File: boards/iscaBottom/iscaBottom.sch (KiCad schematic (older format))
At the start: 30 parts, among them J1 CONN_01X36, J2 CONN_01X36, J3 CONN_01X36

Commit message: iscaBottom: v2 electricly complete
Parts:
- RTD15: footprint footprints:4wire_SMDsolder -> footprints:4wire_SMDsolder_reverse
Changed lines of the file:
@@
 LIBS:valves
 LIBS:lib_iscaBottom
+LIBS:iscaBottom-cache
 EELAYER 25 0
 EELAYER END
@@
 F 0 "RTD15" V 1350 6650 50  0000 C CNN
 F 1 "RTD_4WIRE" V 1450 6650 50  0000 C CNN
-F 2 "footprints:4wire_SMDsolder" H 1550 6650 50  0001 C CNN
+F 2 "footprints:4wire_SMDsolder_reverse" H 1550 6650 50  0001 C CNN
 F 3 "" H 1550 6650 50  0001 C CNN
 	1    1550 6650

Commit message: iscaBottom: board_completed
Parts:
- added R1: 0, Resistors_SMD:R_0603_HandSoldering, symbol R
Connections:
- new net shield: R1.1, R1.2
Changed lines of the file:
@@
 Wire Wire Line
 	1850 8000 2100 8000
+Wire Wire Line
+	3200 800  3750 800
+Text Label 3450 800  0    60   ~ 0
+shield
+$Comp
+L R R1
+U 1 1 59ED224A
+P 3450 900
+F 0 "R1" V 3530 900 50  0000 C CNN
+F 1 "0" V 3450 900 50  0000 C CNN
+F 2 "Resistors_SMD:R_0603_HandSoldering" V 3380 900 50  0001 C CNN
+F 3 "" H 3450 900 50  0001 C CNN
+	1    3450 900
+	0    1    1    0
+$EndComp
+Wire Wire Line
+	3750 800  3750 900
+Wire Wire Line
+	3750 900  3600 900
+Wire Wire Line
+	3200 800  3200 900
+Wire Wire Line
+	3200 900  3300 900
 $EndSCHEMATC

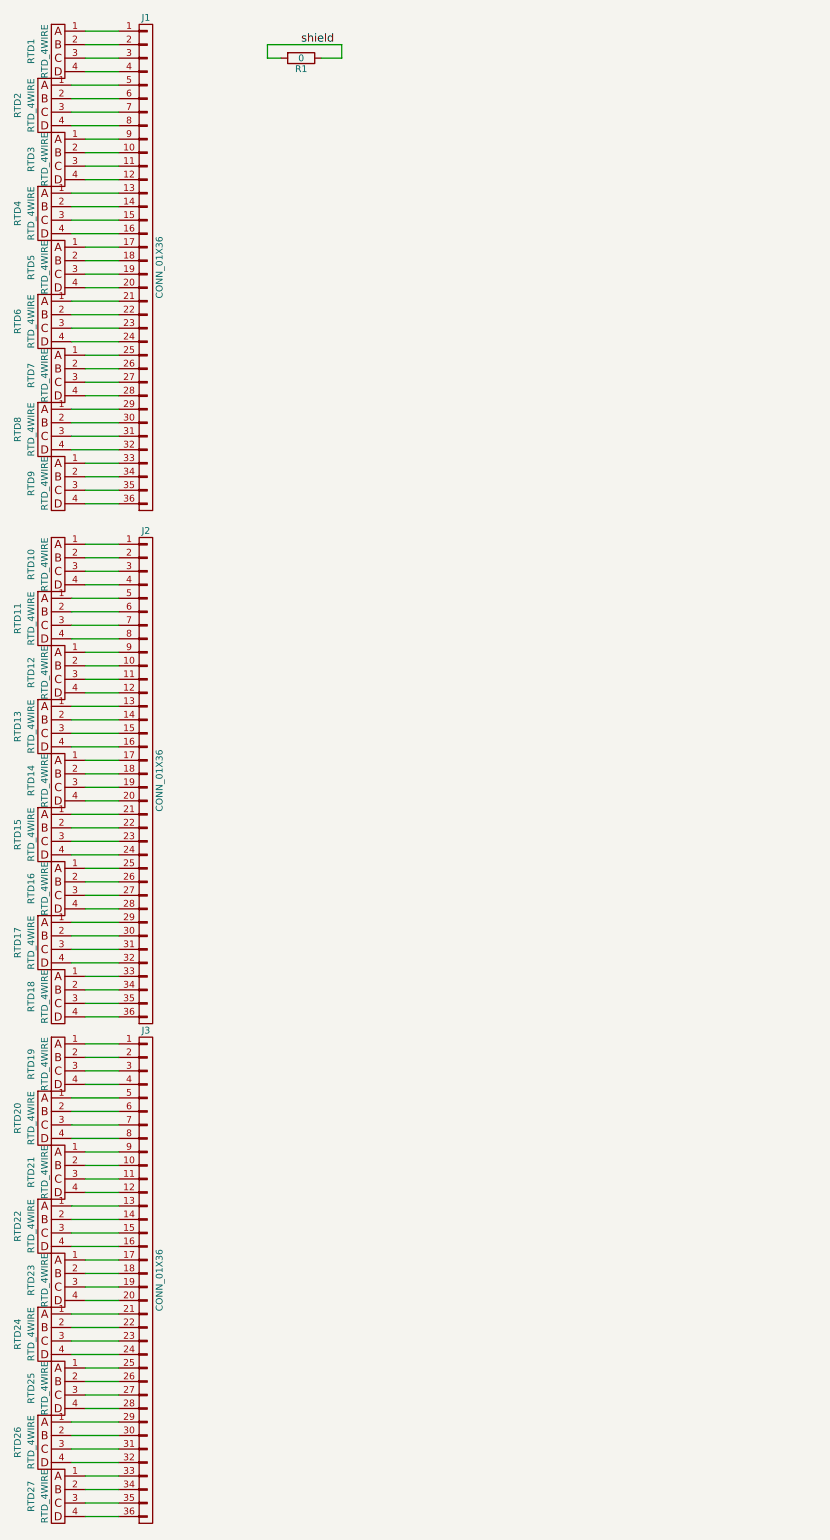
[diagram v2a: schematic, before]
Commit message: addressed all the errors
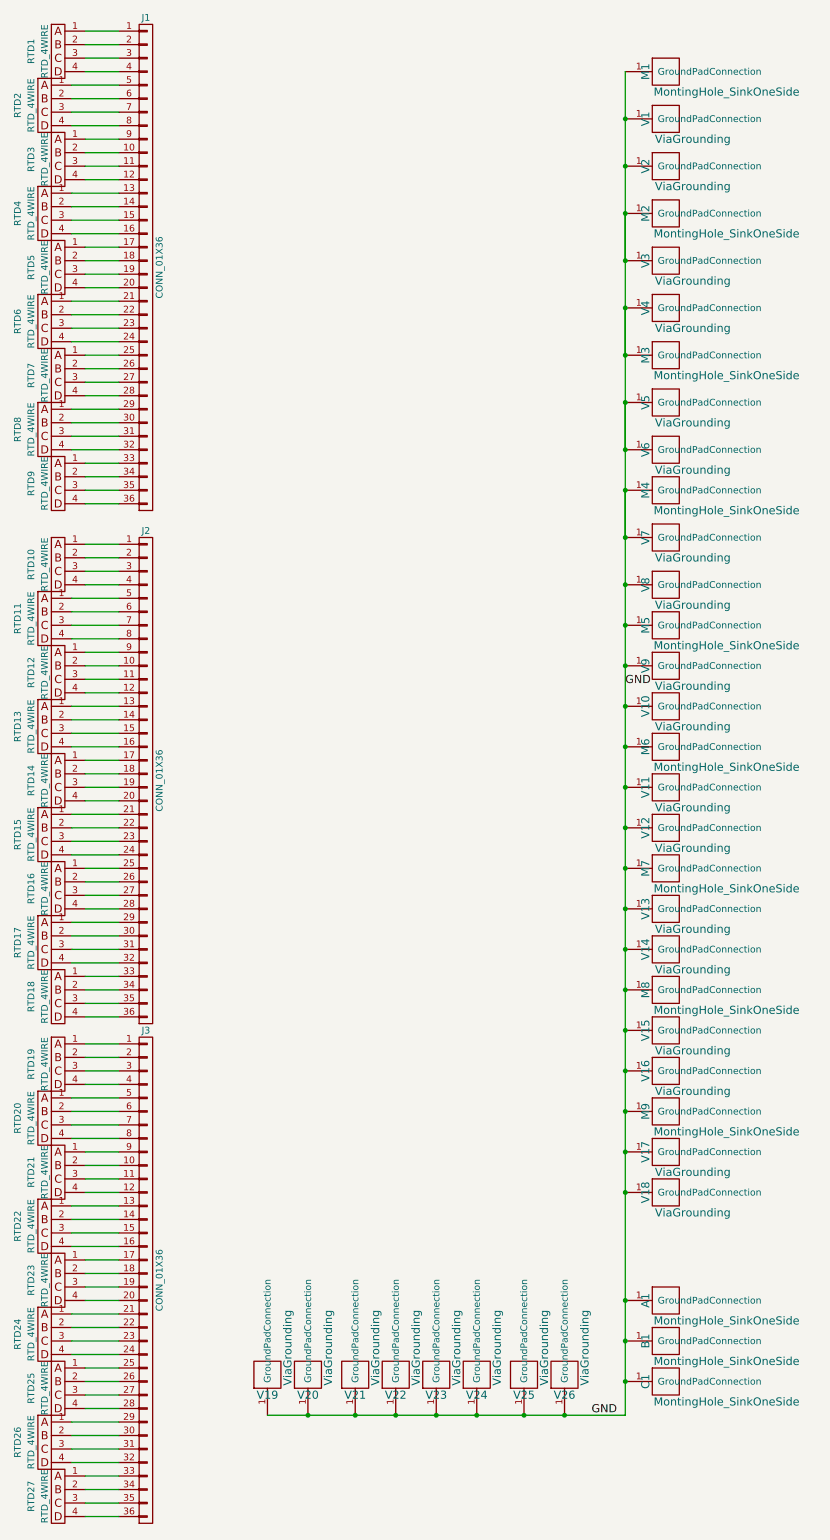
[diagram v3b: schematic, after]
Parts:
- removed R1: 0, Resistors_SMD:R_0603_HandSoldering, symbol R
- added A1, B1, C1, M1, M2, M3, M4, M5, M6, M7, M8, M9: MontingHole_SinkOneSide, footprints:MountingHoleM2_2.2mm_oneSided, symbol MontingHole_SinkOneSide
- added V1, V10, V11, V12, V13, V14, V15, V16, V17, V18, V19, V2, V20, V21, V22, V23, V24, V25, V26, V3, V4, V5, V6, V7, V8, V9: ViaGrounding, footprints:GroundingVia, symbol ViaGrounding
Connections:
- new net GND: A1.1 (GroundPadConnection), B1.1 (GroundPadConnection), C1.1 (GroundPadConnection), M1.1 (GroundPadConnection), M2.1 (GroundPadConnection), M3.1 (GroundPadConnection), M4.1 (GroundPadConnection), M5.1 (GroundPadConnection), M6.1 (GroundPadConnection), M7.1 (GroundPadConnection), M8.1 (GroundPadConnection), M9.1 (GroundPadConnection), V1.1 (GroundPadConnection), V10.1 (GroundPadConnection), V11.1 (GroundPadConnection), V12.1 (GroundPadConnection), V13.1 (GroundPadConnection), V14.1 (GroundPadConnection), V15.1 (GroundPadConnection), V16.1 (GroundPadConnection), V17.1 (GroundPadConnection), V18.1 (GroundPadConnection), V19.1 (GroundPadConnection), V2.1 (GroundPadConnection), V20.1 (GroundPadConnection), V21.1 (GroundPadConnection), V22.1 (GroundPadConnection), V23.1 (GroundPadConnection), V24.1 (GroundPadConnection), V25.1 (GroundPadConnection), V26.1 (GroundPadConnection), V3.1 (GroundPadConnection), V4.1 (GroundPadConnection), V5.1 (GroundPadConnection), V6.1 (GroundPadConnection), V7.1 (GroundPadConnection), V8.1 (GroundPadConnection), V9.1 (GroundPadConnection)
